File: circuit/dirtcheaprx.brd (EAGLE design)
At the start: 25.4 x 27 mm, 20 parts, among them IC1 MCP1700

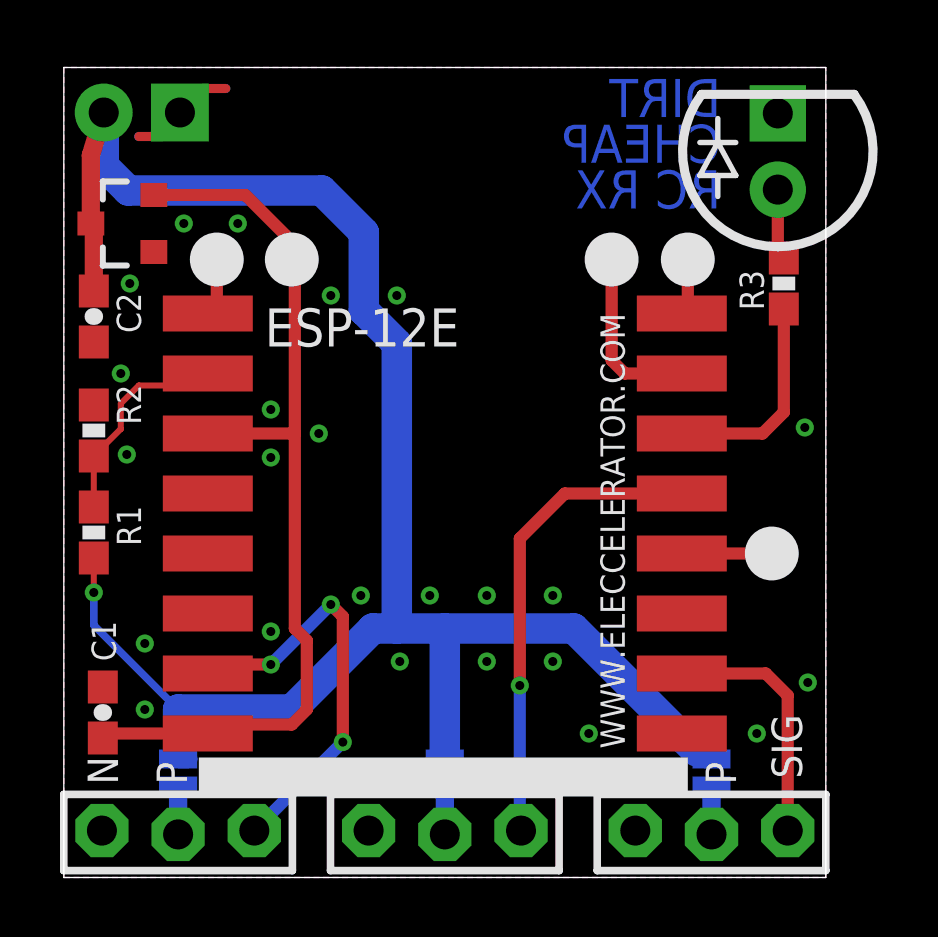
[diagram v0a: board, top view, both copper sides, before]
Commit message: GPIO15 needs to be pulled down, I missed the memo...
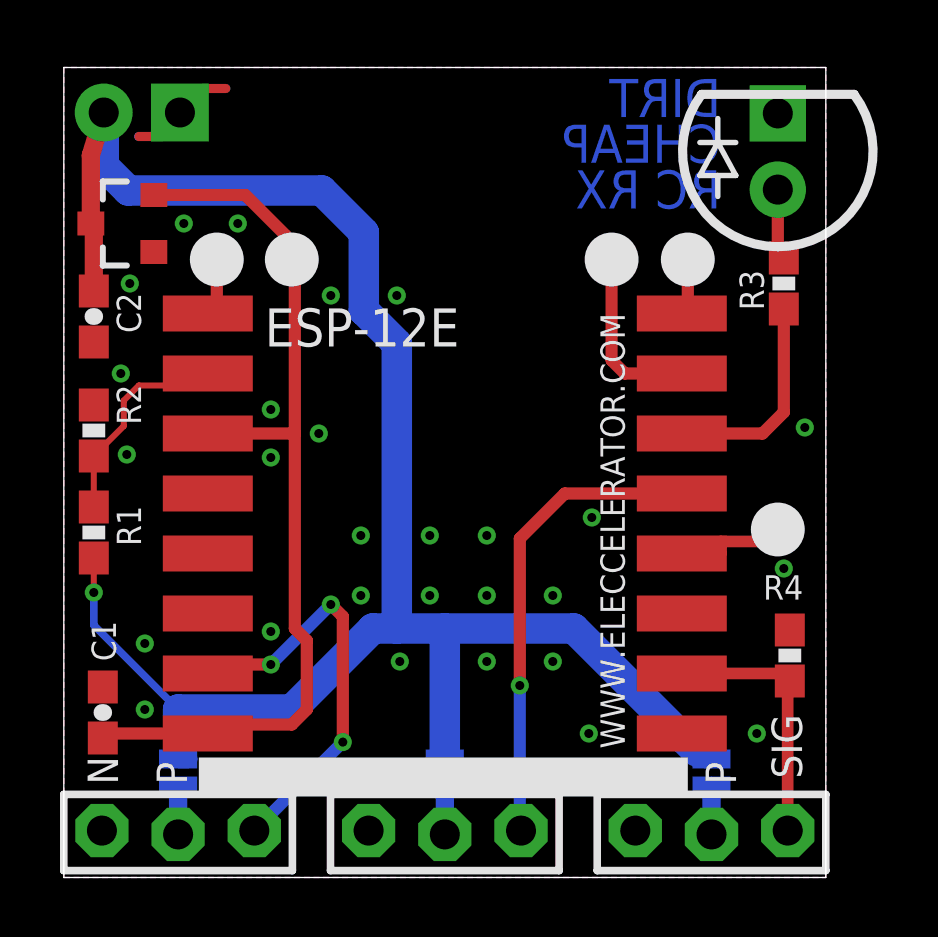
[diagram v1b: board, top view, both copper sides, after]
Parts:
- added R4: 7K5Ω, dirtcheaprx:0603-RES
- moved TP4 0.82 mm to (23.8, 11.6)
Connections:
- net GND: now also R4.1
- net SIG-RIGHT: now also R4.2
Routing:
- net N$11: track 3.00 -> 3.74 mm
- net GND: vias 24 -> 28
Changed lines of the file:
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@@
 <text x="7.6" y="19.5" size="0.8128" layer="26" ratio="10" rot="MR270" align="center-left">+3V3</text>
 <text x="5.1" y="19.4" size="0.8128" layer="26" ratio="10" rot="MR270" align="center-left">RST</text>
-<text x="23.6" y="12" size="0.8128" layer="26" ratio="10" rot="MR90" align="center-left">BOOT</text>
+<text x="23.8" y="12.8" size="0.8128" layer="26" ratio="10" rot="MR90" align="center-left">BOOT</text>
 <text x="20.8" y="19.5" size="0.8128" layer="26" ratio="10" rot="MR270" align="center-left">TX</text>
 <text x="18.2" y="19.5" size="0.8128" layer="26" ratio="10" rot="MR270" align="center-left">RX</text>
@@
 <attribute name="TP_SIGNAL_NAME" value="" x="16.99" y="18.06" size="1" layer="37"/>
 </element>
-<element name="TP4" library="dirtcheaprx" package="P1-13" value="TPPAD1-13" x="23.6" y="10.8" smashed="yes">
-<attribute name="TP_SIGNAL_NAME" value="" x="22.33" y="8.26" size="1" layer="37"/>
+<element name="TP4" library="dirtcheaprx" package="P1-13" value="TPPAD1-13" x="23.8" y="11.6" smashed="yes">
+<attribute name="TP_SIGNAL_NAME" value="" x="22.53" y="9.06" size="1" layer="37"/>
 </element>
 <element name="TP5" library="dirtcheaprx" package="P1-13" value="TPPAD1-13" x="7.6" y="20.6" smashed="yes">
 <attribute name="TP_SIGNAL_NAME" value="" x="6.33" y="18.06" size="1" layer="37"/>
+</element>
+<element name="R4" library="dirtcheaprx" package="0603-RES" value="7K5Ω" x="24.2" y="7.4" smashed="yes" rot="R270">
+<attribute name="NAME" x="23.311" y="9.262" size="0.8128" layer="25" font="vector" ratio="10"/>
+<attribute name="VALUE" x="23.057" y="8.416" size="0.4064" layer="27" font="vector" rot="R270"/>
 </element>
 </elements>
@@
 <via x="16.3" y="9.4" extent="1-16" drill="0.3" shape="octagon"/>
 <via x="16.3" y="7.2" extent="1-16" drill="0.3" shape="octagon"/>
-<via x="24.8" y="6.5" extent="1-16" drill="0.3" shape="octagon"/>
 <via x="2.7" y="5.6" extent="1-16" drill="0.3" shape="octagon"/>
 <via x="17.5" y="4.8" extent="1-16" drill="0.3" shape="octagon"/>
+<contactref element="R4" pad="1"/>
+<via x="9.9" y="11.4" extent="1-16" drill="0.3" shape="octagon"/>
+<via x="12.2" y="11.4" extent="1-16" drill="0.3" shape="octagon"/>
+<via x="14.1" y="11.4" extent="1-16" drill="0.3" shape="octagon"/>
+<via x="17.6" y="12" extent="1-16" drill="0.3" shape="octagon"/>
+<via x="24" y="10.3" extent="1-16" drill="0.3" shape="octagon"/>
 </signal>
 <signal name="ADC">
@@
 <contactref element="R2" pad="2"/>
 <contactref element="R1" pad="1"/>
-<wire x1="1" y1="14.05" x2="1.9" y2="14.95" width="0.2032" layer="1"/>
+<wire x1="1" y1="14.05" x2="2" y2="15.05" width="0.2032" layer="1"/>
 <wire x1="1" y1="14.05" x2="1" y2="12.35" width="0.2032" layer="1"/>
-<wire x1="1.9" y1="14.95" x2="1.9" y2="15.8" width="0.2032" layer="1"/>
-<wire x1="1.9" y1="15.8" x2="2.5" y2="16.4" width="0.2032" layer="1"/>
+<wire x1="2" y1="15.05" x2="2" y2="15.9" width="0.2032" layer="1"/>
+<wire x1="2" y1="15.9" x2="2.5" y2="16.4" width="0.2032" layer="1"/>
 <wire x1="2.5" y1="16.4" x2="4" y2="16.4" width="0.2032" layer="1"/>
 <wire x1="4" y1="16.4" x2="4.8" y2="16.8" width="0.2032" layer="1"/>
@@
 <signal name="SIG-RIGHT">
 <contactref element="SERVO1" pad="SIG"/>
-<wire x1="23.4" y1="6.8" x2="24.13" y2="6.07" width="0.4064" layer="1"/>
-<wire x1="24.13" y1="6.07" x2="24.13" y2="1.5635" width="0.4064" layer="1"/>
 <contactref element="U1" pad="GPIO15"/>
-<wire x1="23.4" y1="6.8" x2="20.6" y2="6.8" width="0.4064" layer="1"/>
+<contactref element="R4" pad="2"/>
+<wire x1="20.6" y1="6.8" x2="24.1" y2="6.8" width="0.39" layer="1"/>
+<wire x1="24.1" y1="6.8" x2="24.2" y2="6.55" width="0.39" layer="1"/>
+<wire x1="24.13" y1="1.5635" x2="24.13" y2="6.12" width="0.39" layer="1"/>
+<wire x1="24.13" y1="6.12" x2="24.2" y2="6.55" width="0.39" layer="1"/>
 </signal>
 <signal name="N$8">
@@
 <contactref element="U1" pad="GPIO0"/>
 <contactref element="TP4" pad="TP"/>
-<wire x1="20.6" y1="10.8" x2="23.6" y2="10.8" width="0.4064" layer="1"/>
+<wire x1="20.6" y1="10.8" x2="21.9" y2="10.8" width="0.39" layer="1"/>
+<wire x1="21.9" y1="10.8" x2="21.9" y2="11.2" width="0.39" layer="1"/>
+<wire x1="21.9" y1="11.2" x2="23.3" y2="11.2" width="0.39" layer="1"/>
+<wire x1="23.3" y1="11.2" x2="23.8" y2="11.6" width="0.39" layer="1"/>
 </signal>
 <signal name="LED">

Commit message: corrected GPIO4 and GPIO5 mixup in PCBs
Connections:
- net LED: now also U1.GPIO5; no longer U1.GPIO4
- net SIG-WEAP: now also U1.GPIO4; no longer U1.GPIO5
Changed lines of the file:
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@@
 </signal>
 <signal name="LED">
-<contactref element="U1" pad="GPIO4"/>
+<contactref element="U1" pad="GPIO5"/>
 <contactref element="R3" pad="1"/>
 <wire x1="20.6" y1="14.8" x2="23.29289375" y2="14.8" width="0.4064" layer="1"/>
@@
 <signal name="SIG-WEAP">
 <contactref element="SERVO2" pad="SIG"/>
-<contactref element="U1" pad="GPIO5"/>
+<contactref element="U1" pad="GPIO4"/>
 <wire x1="20.6" y1="12.8" x2="16.7" y2="12.8" width="0.4064" layer="1"/>
 <wire x1="16.7" y1="12.8" x2="15.2" y2="11.3" width="0.4064" layer="1"/>
